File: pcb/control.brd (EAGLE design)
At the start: 90 x 100 mm, 107 parts, among them J1 PCC-SMP, J10 USB-C, J2 2X1_2.54, J3 PCC-SMP, J4 MICROSD, J5 2EDG-2P, J6 3X1_2.54, J7 4P-PC-FAN, J8 2EDG-2P, J9 2EDG-2P, M1 HM-11, Q1 BC817-40, Q2 BC817-40, Q3 BC817-40, Q4 BC817-40, U1 MIC4682, U10 EFM32GG11B4XX_Q100, U2 MCP9600, U3 SST26VF064B, U4 MCP9600, U5 74LVC1G17, U6 CP2102N, U7 ER-TFT035-6BOT, U8 74LVC1G17, U9 74LVC1G17, Y1 8MHz, Y2 32.768KHz

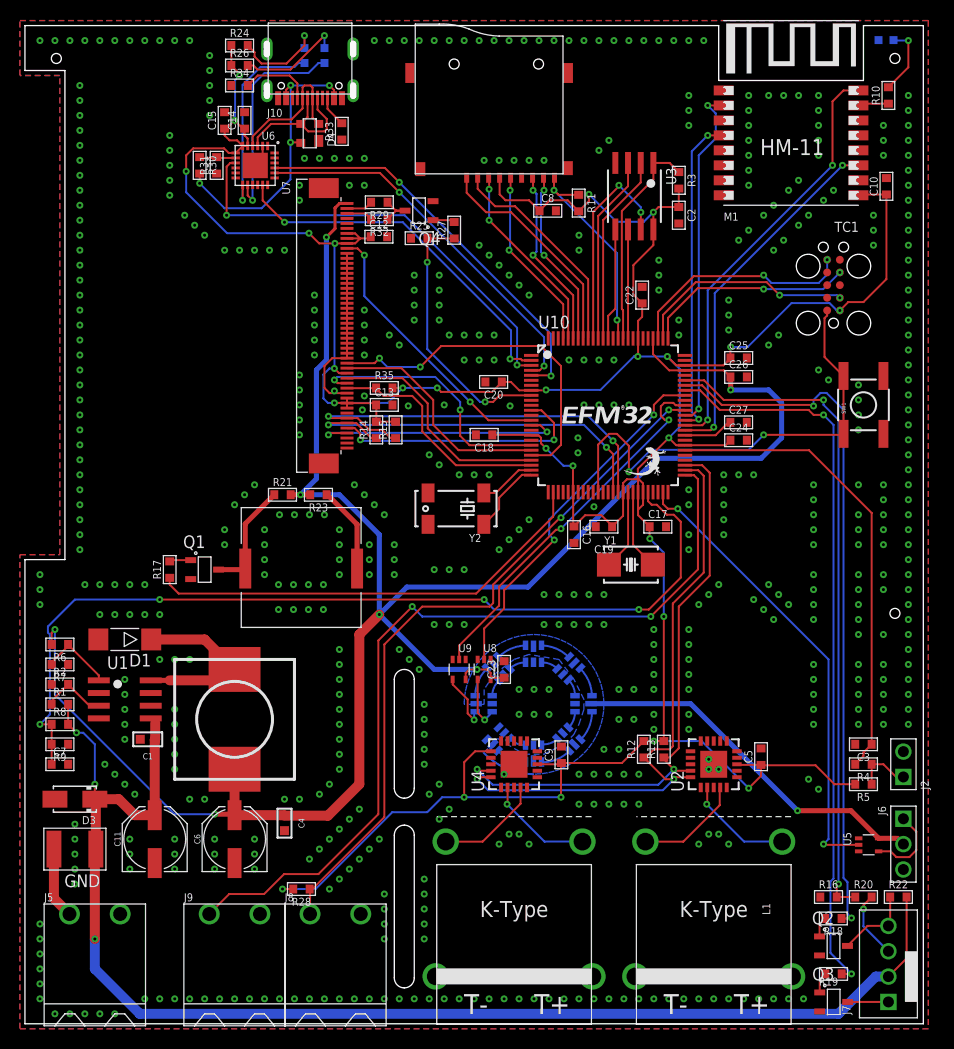
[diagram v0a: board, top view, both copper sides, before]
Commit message: finished silkscreen and ssr pcb
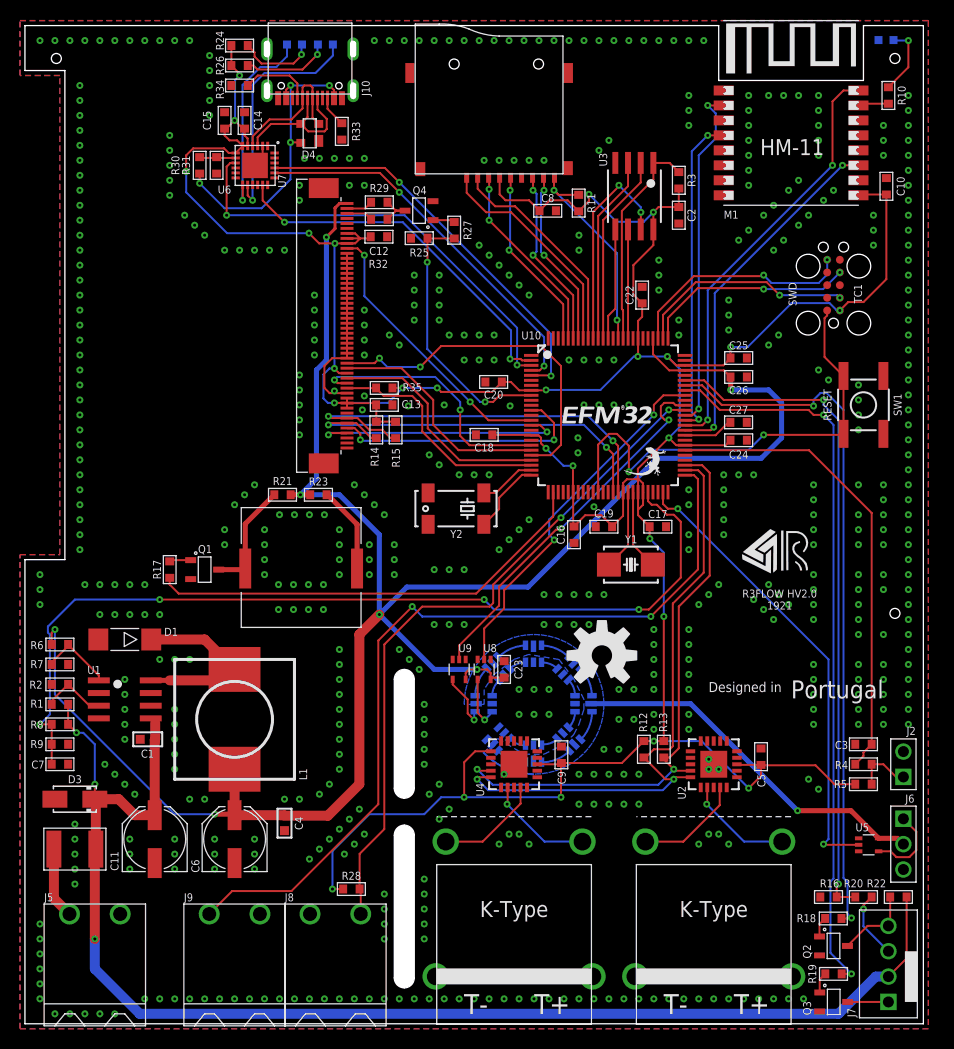
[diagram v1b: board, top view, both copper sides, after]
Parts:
- added U$1: (no value), Utility > Silkscreen:DESIGNEDINPT
- added U$2: (no value), Utility > Silkscreen:OSHW-LOGO-L
- added U$3: (no value), Utility > Silkscreen:RAFAEL_SILVA_5MM_ALT_3
- moved R28 5.00 mm to (32.7, 13.5)
- moved D5 1.49 mm to (27.0, 98.1), turned to 270 degrees
- moved D6 1.10 mm to (30.1, 98.1), turned to 90 degrees
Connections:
- net GND: now also J8.P$1; no longer J8.P$2
- net WTIM1-CC1-ZERO-CROSS: now also J8.P$2; no longer J8.P$1
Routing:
- net 3.3V: track 358.1 -> 355.3 mm
- net N$15: track 21.4 -> 23.7 mm
- net WTIM1-CC1-ZERO-CROSS: track 71.2 -> 69.1 mm
- net N$19: track 9.67 -> 7.82 mm
- net N$16: track 10.5 -> 8.78 mm
- net PRS-CH11-SSR-OUT: track 84.8 -> 84.2 mm
- net GND: vias 570 -> 567
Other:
- outline, holes or cut-outs redrawn
- board text added: "R3FLOW HV2.0 1921"
- board text added: "RESET"
- board text added: "SWD"
- board text added: "rx"
- board text added: "tx"

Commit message: pcb order
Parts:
- added U$4: (no value), Utility > Silkscreen:GECKO_POLY
- U$3: device Utility > Silkscreen:RAFAEL_SILVA_5MM_ALT_3 -> Utility > Silkscreen:RAFAEL_SILVA_10MM_ALT
- moved U$3 8.64 mm to (68.5, 39.5)
- moved U$1 3.64 mm to (75.1, 36.1)
- moved U$2 1.41 mm to (56.8, 35.9)
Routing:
- net GND: vias 567 -> 731
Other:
- board text added: "12v"
- board text added: "gnd"
- board text added: "ssr out"
- board text added: "zero cross"

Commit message: sync
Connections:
- new net TIM0-CC0-BUZZ: U10.27
- net TIM0-CC2-BUZZ: no longer U10.27
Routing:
- net TIM0-CC2-BUZZ: track 45.1 -> 42.7 mm
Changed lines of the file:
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@@
 <drawing>
 <settings>
-<setting alwaysvectorfont="yes"/>
+<setting alwaysvectorfont="no"/>
 <setting verticaltext="up"/>
 </settings>
@@
 <signal name="TIM0-CC2-BUZZ">
 <contactref element="R17" pad="P$1"/>
-<contactref element="U10" pad="27"/>
 <wire x1="14.5" y1="44.677" x2="14.5" y2="44" width="0.2" layer="1"/>
-<wire x1="52.92" y1="53.26" x2="52.92" y2="50.82" width="0.2" layer="1"/>
 <wire x1="15.4" y1="43.1" x2="14.5" y2="44" width="0.2" layer="1"/>
 <wire x1="52.92" y1="50.82" x2="45.2" y2="43.1" width="0.2" layer="1"/>
@@
 <via x="57" y="51.8" extent="1-16" drill="0.3"/>
 </signal>
+<signal name="TIM0-CC0-BUZZ">
+<contactref element="U10" pad="27"/>
+</signal>
 </signals>
